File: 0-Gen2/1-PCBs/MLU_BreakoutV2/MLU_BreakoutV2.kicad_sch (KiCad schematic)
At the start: 17 parts, among them J1 SBH11-PBPC-D10-ST-BK, J2 SBH11-PBPC-D10-ST-BK, U1 Teensy4.1

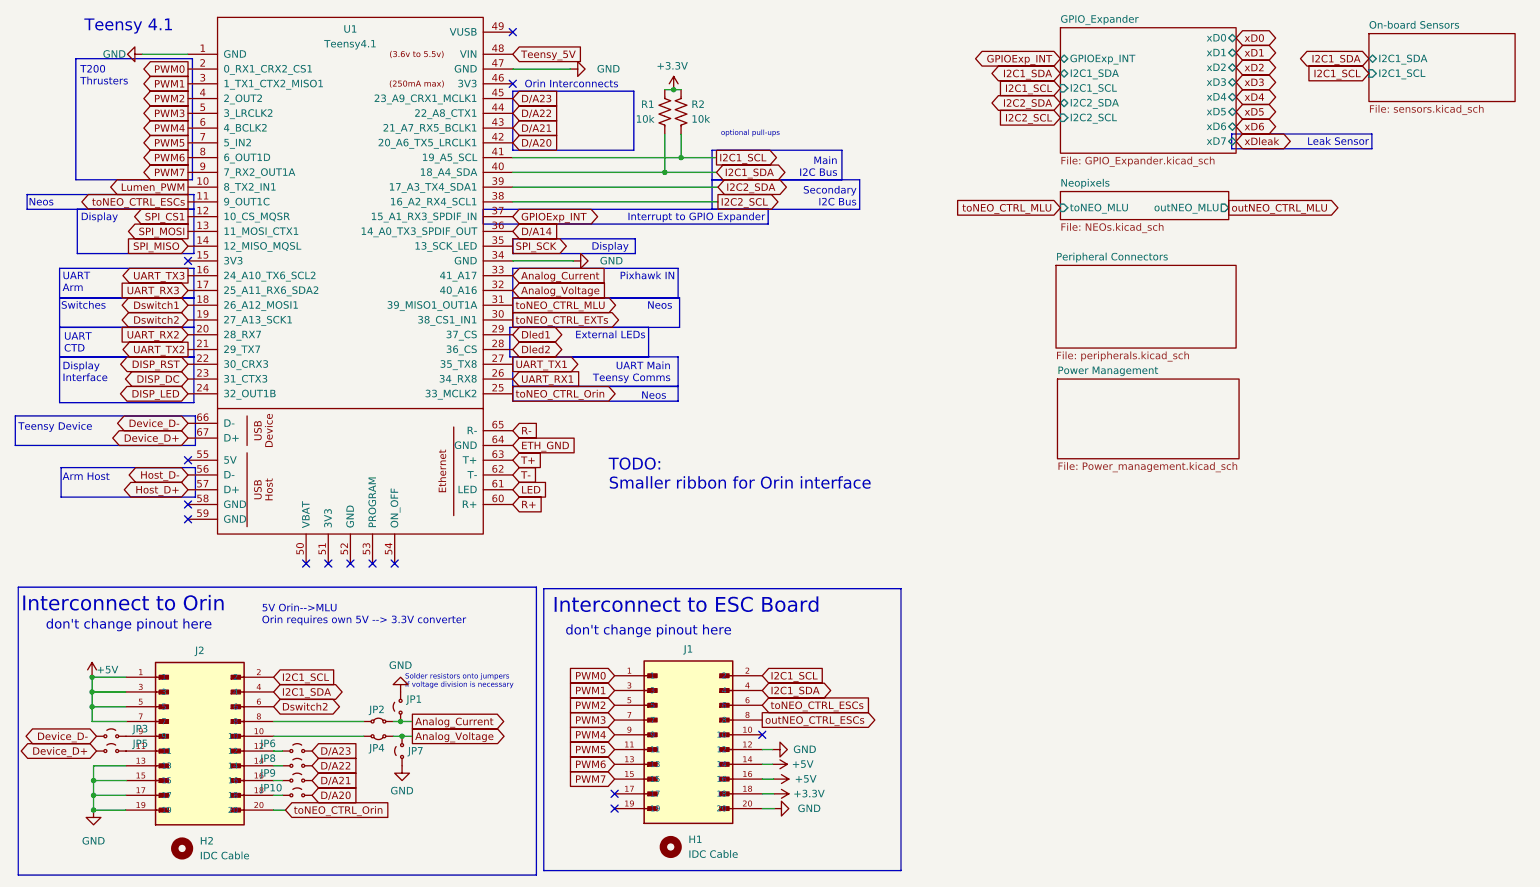
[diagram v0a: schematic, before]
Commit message: [bugfix] rescued footprints
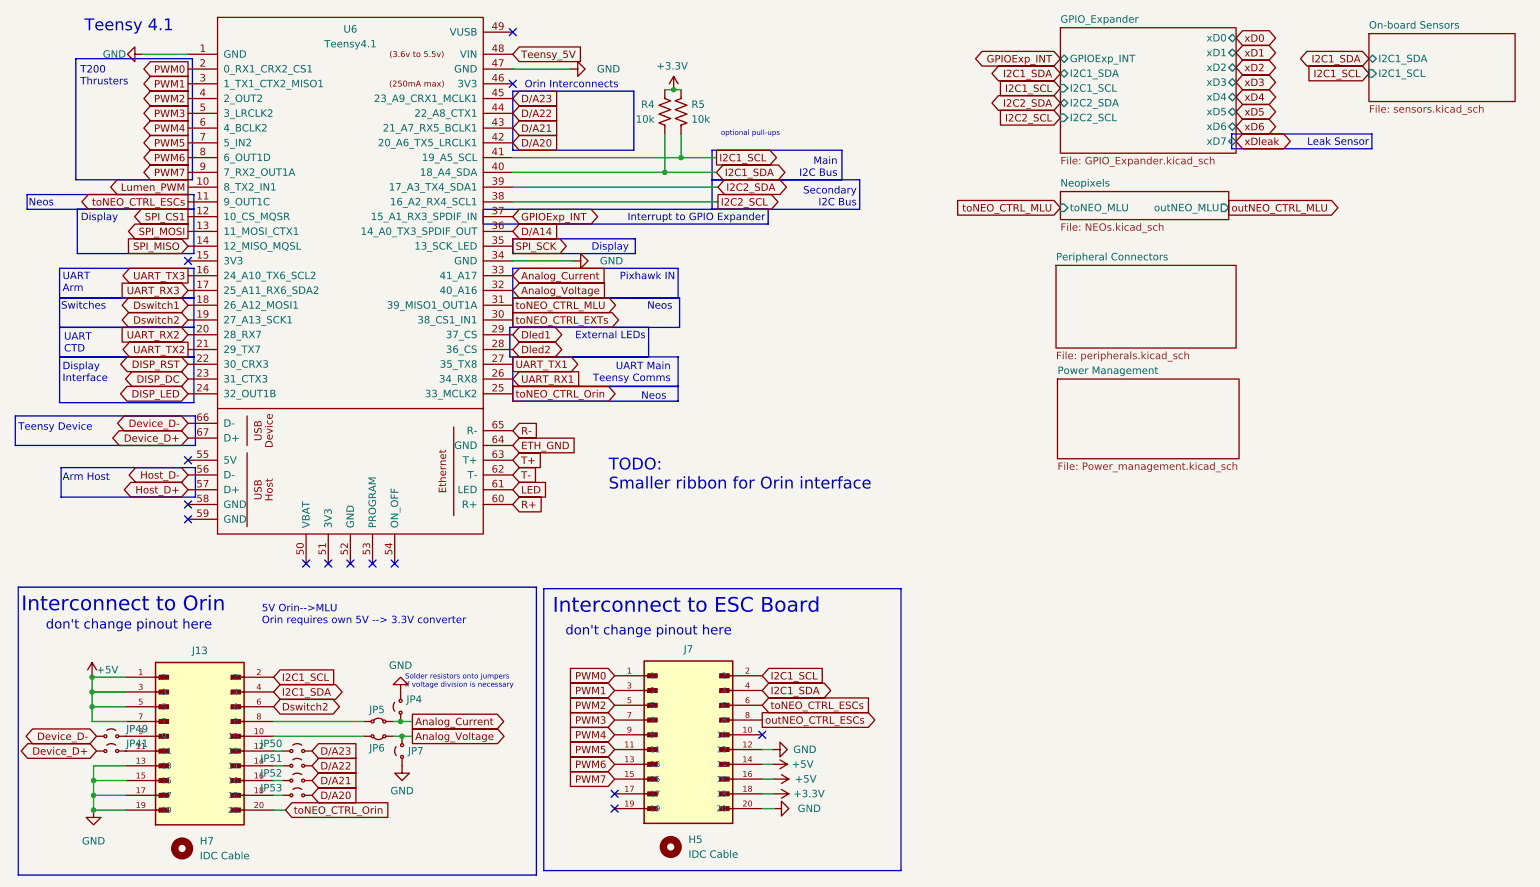
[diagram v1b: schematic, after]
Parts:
- renumbered H1 to H5, H2 to H7, J2 to J13, J1 to J7, JP1 to JP4, JP5 to JP41, JP3 to JP49, JP2 to JP5, JP6 to JP50, JP8 to JP51, JP9 to JP52, JP10 to JP53, JP4 to JP6, R1 to R4, R2 to R5, U1 to U6
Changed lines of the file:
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@@
 		(dnp no)
 		(fields_autoplaced yes)
-		(property "Reference" "#PWR04"
+		(property "Reference" "#PWR039"
 			(at 116.84 56.388 0)
 			(effects
@@
 			(project "MLU_BreakoutV2"
 				(path "/55121ba7-5d22-4fe3-93aa-7f76d75b410c"
-					(reference "#PWR04")
+					(reference "#PWR039")
 					(unit 1)
 				)
@@
 		(on_board yes)
 		(dnp no)
-		(property "Reference" "U1"
+		(property "Reference" "U6"
 			(at 72.136 16.51 0)
 			(effects
@@
 			(project "MLU_BreakoutV2"
 				(path "/55121ba7-5d22-4fe3-93aa-7f76d75b410c"
-					(reference "U1")
+					(reference "U6")
 					(unit 1)
 				)
@@
 		(on_board yes)
 		(dnp no)
-		(property "Reference" "#PWR03"
+		(property "Reference" "#PWR027"
 			(at 127.762 30.988 0)
 			(effects
@@
 			(project "MLU_BreakoutV2"
 				(path "/55121ba7-5d22-4fe3-93aa-7f76d75b410c"
-					(reference "#PWR03")
+					(reference "#PWR027")
 					(unit 1)
 				)
@@
 		(on_board yes)
 		(dnp no)
-		(property "Reference" "R1"
+		(property "Reference" "R4"
 			(at 124.46 29.4639 0)
 			(effects
@@
 			(project "MLU_BreakoutV2"
 				(path "/55121ba7-5d22-4fe3-93aa-7f76d75b410c"
-					(reference "R1")
+					(reference "R4")
 					(unit 1)
 				)
@@
 		(dnp no)
 		(fields_autoplaced yes)
-		(property "Reference" "H2"
+		(property "Reference" "H7"
 			(at 46.228 156.2099 0)
 			(effects
@@
 			(project "MLU_BreakoutV2"
 				(path "/55121ba7-5d22-4fe3-93aa-7f76d75b410c"
-					(reference "H2")
+					(reference "H7")
 					(unit 1)
 				)
@@
 		(dnp no)
 		(fields_autoplaced yes)
-		(property "Reference" "#PWR09"
+		(property "Reference" "#PWR063"
 			(at 81.026 149.606 0)
 			(effects
@@
 			(project ""
 				(path "/55121ba7-5d22-4fe3-93aa-7f76d75b410c"
-					(reference "#PWR09")
+					(reference "#PWR063")
 					(unit 1)
 				)
@@
 		(dnp no)
 		(fields_autoplaced yes)
-		(property "Reference" "#PWR06"
+		(property "Reference" "#PWR061"
 			(at 80.772 124.206 0)
 			(effects
@@
 			(project ""
 				(path "/55121ba7-5d22-4fe3-93aa-7f76d75b410c"
-					(reference "#PWR06")
+					(reference "#PWR061")
 					(unit 1)
 				)
@@
 		(dnp no)
 		(fields_autoplaced yes)
-		(property "Reference" "#PWR010"
+		(property "Reference" "#PWR030"
 			(at 141.224 145.542 0)
 			(effects
@@
 			(project "MLU_BreakoutV2"
 				(path "/55121ba7-5d22-4fe3-93aa-7f76d75b410c"
-					(reference "#PWR010")
+					(reference "#PWR030")
 					(unit 1)
 				)
@@
 		(on_board yes)
 		(dnp no)
-		(property "Reference" "JP2"
+		(property "Reference" "JP5"
 			(at 76.708 133.604 0)
 			(effects
@@
 			(project ""
 				(path "/55121ba7-5d22-4fe3-93aa-7f76d75b410c"
-					(reference "JP2")
+					(reference "JP5")
 					(unit 1)
 				)
@@
 		(on_board yes)
 		(dnp no)
-		(property "Reference" "#PWR05"
+		(property "Reference" "#PWR060"
 			(at 27.686 131.826 0)
 			(effects
@@
 			(project "MLU_BreakoutV2"
 				(path "/55121ba7-5d22-4fe3-93aa-7f76d75b410c"
-					(reference "#PWR05")
+					(reference "#PWR060")
 					(unit 1)
 				)
@@
 		(on_board yes)
 		(dnp no)
-		(property "Reference" "JP6"
+		(property "Reference" "JP50"
 			(at 56.642 139.446 0)
 			(effects
@@
 			(project "MLU_BreakoutV2"
 				(path "/55121ba7-5d22-4fe3-93aa-7f76d75b410c"
-					(reference "JP6")
+					(reference "JP50")
 					(unit 1)
 				)
@@
 		(dnp no)
 		(fields_autoplaced yes)
-		(property "Reference" "#PWR07"
+		(property "Reference" "#PWR028"
 			(at 151.13 140.462 0)
 			(effects
@@
 			(project "MLU_BreakoutV2"
 				(path "/55121ba7-5d22-4fe3-93aa-7f76d75b410c"
-					(reference "#PWR07")
+					(reference "#PWR028")
 					(unit 1)
 				)
@@
 		(on_board yes)
 		(dnp no)
-		(property "Reference" "JP1"
+		(property "Reference" "JP4"
 			(at 81.788 131.826 90)
 			(effects
@@
 			(project ""
 				(path "/55121ba7-5d22-4fe3-93aa-7f76d75b410c"
-					(reference "JP1")
+					(reference "JP4")
 					(unit 1)
 				)
@@
 		(on_board yes)
 		(dnp no)
-		(property "Reference" "R2"
+		(property "Reference" "R5"
 			(at 130.81 29.4639 0)
 			(effects
@@
 			(project "MLU_BreakoutV2"
 				(path "/55121ba7-5d22-4fe3-93aa-7f76d75b410c"
-					(reference "R2")
+					(reference "R5")
 					(unit 1)
 				)
@@
 		(on_board yes)
 		(dnp no)
-		(property "Reference" "J2"
+		(property "Reference" "J13"
 			(at 46.228 123.444 0)
 			(effects
@@
 			(project "MLU_BreakoutV2"
 				(path "/55121ba7-5d22-4fe3-93aa-7f76d75b410c"
-					(reference "J2")
+					(reference "J13")
 					(unit 1)
 				)
@@
 		(on_board yes)
 		(dnp no)
-		(property "Reference" "#PWR02"
+		(property "Reference" "#PWR026"
 			(at 116.332 23.368 0)
 			(effects
@@
 			(project "MLU_BreakoutV2"
 				(path "/55121ba7-5d22-4fe3-93aa-7f76d75b410c"
-					(reference "#PWR02")
+					(reference "#PWR026")
 					(unit 1)
 				)
@@
 		(on_board yes)
 		(dnp no)
-		(property "Reference" "JP10"
+		(property "Reference" "JP53"
 			(at 56.642 147.066 0)
 			(effects
@@
 			(project "MLU_BreakoutV2"
 				(path "/55121ba7-5d22-4fe3-93aa-7f76d75b410c"
-					(reference "JP10")
+					(reference "JP53")
 					(unit 1)
 				)
@@
 		(on_board yes)
 		(dnp no)
-		(property "Reference" "J1"
+		(property "Reference" "J7"
 			(at 130.302 123.19 0)
 			(effects
@@
 			(project "MLU_BreakoutV2"
 				(path "/55121ba7-5d22-4fe3-93aa-7f76d75b410c"
-					(reference "J1")
+					(reference "J7")
 					(unit 1)
 				)
@@
 		(on_board yes)
 		(dnp no)
-		(property "Reference" "JP4"
+		(property "Reference" "JP6"
 			(at 76.708 140.208 0)
 			(effects
@@
 			(project "MLU_BreakoutV2"
 				(path "/55121ba7-5d22-4fe3-93aa-7f76d75b410c"
-					(reference "JP4")
+					(reference "JP6")
 					(unit 1)
 				)
@@
 		(on_board yes)
 		(dnp no)
-		(property "Reference" "JP8"
+		(property "Reference" "JP51"
 			(at 56.642 141.986 0)
 			(effects
@@
 			(project "MLU_BreakoutV2"
 				(path "/55121ba7-5d22-4fe3-93aa-7f76d75b410c"
-					(reference "JP8")
+					(reference "JP51")
 					(unit 1)
 				)
@@
 		(on_board yes)
 		(dnp no)
-		(property "Reference" "JP3"
+		(property "Reference" "JP49"
 			(at 37.338 136.906 0)
 			(effects
@@
 			(project "MLU_BreakoutV2"
 				(path "/55121ba7-5d22-4fe3-93aa-7f76d75b410c"
-					(reference "JP3")
+					(reference "JP49")
 					(unit 1)
 				)
@@
 		(dnp no)
 		(fields_autoplaced yes)
-		(property "Reference" "#PWR012"
+		(property "Reference" "#PWR034"
 			(at 151.384 150.622 0)
 			(effects
@@
 			(project "MLU_BreakoutV2"
 				(path "/55121ba7-5d22-4fe3-93aa-7f76d75b410c"
-					(reference "#PWR012")
+					(reference "#PWR034")
 					(unit 1)
 				)
@@
 		(dnp no)
 		(fields_autoplaced yes)
-		(property "Reference" "#PWR01"
+		(property "Reference" "#PWR025"
 			(at 29.972 20.828 0)
 			(effects
@@
 			(project ""
 				(path "/55121ba7-5d22-4fe3-93aa-7f76d75b410c"
-					(reference "#PWR01")
+					(reference "#PWR025")
 					(unit 1)
 				)
@@
 		(on_board yes)
 		(dnp no)
-		(property "Reference" "JP5"
+		(property "Reference" "JP41"
 			(at 37.338 139.446 0)
 			(effects
@@
 			(project "MLU_BreakoutV2"
 				(path "/55121ba7-5d22-4fe3-93aa-7f76d75b410c"
-					(reference "JP5")
+					(reference "JP41")
 					(unit 1)
 				)
@@
 		(dnp no)
 		(fields_autoplaced yes)
-		(property "Reference" "#PWR013"
+		(property "Reference" "#PWR064"
 			(at 27.94 157.226 0)
 			(effects
@@
 			(project "MLU_BreakoutV2"
 				(path "/55121ba7-5d22-4fe3-93aa-7f76d75b410c"
-					(reference "#PWR013")
+					(reference "#PWR064")
 					(unit 1)
 				)
@@
 		(dnp no)
 		(fields_autoplaced yes)
-		(property "Reference" "#PWR011"
+		(property "Reference" "#PWR032"
 			(at 141.224 148.082 0)
 			(effects
@@
 			(project "MLU_BreakoutV2"
 				(path "/55121ba7-5d22-4fe3-93aa-7f76d75b410c"
-					(reference "#PWR011")
+					(reference "#PWR032")
 					(unit 1)
 				)
@@
 		(dnp no)
 		(fields_autoplaced yes)
-		(property "Reference" "H1"
+		(property "Reference" "H5"
 			(at 130.302 155.9559 0)
 			(effects
@@
 			(project "MLU_BreakoutV2"
 				(path "/55121ba7-5d22-4fe3-93aa-7f76d75b410c"
-					(reference "H1")
+					(reference "H5")
 					(unit 1)
 				)
@@
 		(dnp no)
 		(fields_autoplaced yes)
-		(property "Reference" "#PWR08"
+		(property "Reference" "#PWR029"
 			(at 140.97 143.002 0)
 			(effects
@@
 			(project "MLU_BreakoutV2"
 				(path "/55121ba7-5d22-4fe3-93aa-7f76d75b410c"
-					(reference "#PWR08")
+					(reference "#PWR029")
 					(unit 1)
 				)
@@
 		(on_board yes)
 		(dnp no)
-		(property "Reference" "JP9"
+		(property "Reference" "JP52"
 			(at 56.642 144.526 0)
 			(effects
@@
 			(project "MLU_BreakoutV2"
 				(path "/55121ba7-5d22-4fe3-93aa-7f76d75b410c"
-					(reference "JP9")
+					(reference "JP52")
 					(unit 1)
 				)

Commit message: before restructure
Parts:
- renumbered H5 to H1, H7 to H2, J7 to J1, J13 to J2, JP4 to JP1, JP53 to JP10, JP5 to JP2, JP49 to JP3, JP6 to JP4, JP41 to JP5, JP50 to JP6, JP51 to JP8, JP52 to JP9, R4 to R1, R5 to R2, U6 to U1
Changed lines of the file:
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@@
 		(dnp no)
 		(fields_autoplaced yes)
-		(property "Reference" "#PWR039"
+		(property "Reference" "#PWR04"
 			(at 116.84 56.388 0)
 			(effects
@@
 			(project "MLU_BreakoutV2"
 				(path "/55121ba7-5d22-4fe3-93aa-7f76d75b410c"
-					(reference "#PWR039")
+					(reference "#PWR04")
 					(unit 1)
 				)
@@
 		(on_board yes)
 		(dnp no)
-		(property "Reference" "U6"
+		(property "Reference" "U1"
 			(at 72.136 16.51 0)
 			(effects
@@
 			(project "MLU_BreakoutV2"
 				(path "/55121ba7-5d22-4fe3-93aa-7f76d75b410c"
-					(reference "U6")
+					(reference "U1")
 					(unit 1)
 				)
@@
 		(on_board yes)
 		(dnp no)
-		(property "Reference" "#PWR027"
+		(property "Reference" "#PWR03"
 			(at 127.762 30.988 0)
 			(effects
@@
 			(project "MLU_BreakoutV2"
 				(path "/55121ba7-5d22-4fe3-93aa-7f76d75b410c"
-					(reference "#PWR027")
+					(reference "#PWR03")
 					(unit 1)
 				)
@@
 		(on_board yes)
 		(dnp no)
-		(property "Reference" "R4"
+		(property "Reference" "R1"
 			(at 124.46 29.4639 0)
 			(effects
@@
 			(project "MLU_BreakoutV2"
 				(path "/55121ba7-5d22-4fe3-93aa-7f76d75b410c"
-					(reference "R4")
+					(reference "R1")
 					(unit 1)
 				)
@@
 		(dnp no)
 		(fields_autoplaced yes)
-		(property "Reference" "H7"
+		(property "Reference" "H2"
 			(at 46.228 156.2099 0)
 			(effects
@@
 			(project "MLU_BreakoutV2"
 				(path "/55121ba7-5d22-4fe3-93aa-7f76d75b410c"
-					(reference "H7")
+					(reference "H2")
 					(unit 1)
 				)
@@
 		(dnp no)
 		(fields_autoplaced yes)
-		(property "Reference" "#PWR063"
+		(property "Reference" "#PWR09"
 			(at 81.026 149.606 0)
 			(effects
@@
 			(project ""
 				(path "/55121ba7-5d22-4fe3-93aa-7f76d75b410c"
-					(reference "#PWR063")
+					(reference "#PWR09")
 					(unit 1)
 				)
@@
 		(dnp no)
 		(fields_autoplaced yes)
-		(property "Reference" "#PWR061"
+		(property "Reference" "#PWR06"
 			(at 80.772 124.206 0)
 			(effects
@@
 			(project ""
 				(path "/55121ba7-5d22-4fe3-93aa-7f76d75b410c"
-					(reference "#PWR061")
+					(reference "#PWR06")
 					(unit 1)
 				)
@@
 		(dnp no)
 		(fields_autoplaced yes)
-		(property "Reference" "#PWR030"
+		(property "Reference" "#PWR010"
 			(at 141.224 145.542 0)
 			(effects
@@
 			(project "MLU_BreakoutV2"
 				(path "/55121ba7-5d22-4fe3-93aa-7f76d75b410c"
-					(reference "#PWR030")
+					(reference "#PWR010")
 					(unit 1)
 				)
@@
 		(on_board yes)
 		(dnp no)
-		(property "Reference" "JP5"
+		(property "Reference" "JP2"
 			(at 76.708 133.604 0)
 			(effects
@@
 			(project ""
 				(path "/55121ba7-5d22-4fe3-93aa-7f76d75b410c"
-					(reference "JP5")
+					(reference "JP2")
 					(unit 1)
 				)
@@
 		(on_board yes)
 		(dnp no)
-		(property "Reference" "#PWR060"
+		(property "Reference" "#PWR05"
 			(at 27.686 131.826 0)
 			(effects
@@
 			(project "MLU_BreakoutV2"
 				(path "/55121ba7-5d22-4fe3-93aa-7f76d75b410c"
-					(reference "#PWR060")
+					(reference "#PWR05")
 					(unit 1)
 				)
@@
 		(on_board yes)
 		(dnp no)
-		(property "Reference" "JP50"
+		(property "Reference" "JP6"
 			(at 56.642 139.446 0)
 			(effects
@@
 			(project "MLU_BreakoutV2"
 				(path "/55121ba7-5d22-4fe3-93aa-7f76d75b410c"
-					(reference "JP50")
+					(reference "JP6")
 					(unit 1)
 				)
@@
 		(dnp no)
 		(fields_autoplaced yes)
-		(property "Reference" "#PWR028"
+		(property "Reference" "#PWR07"
 			(at 151.13 140.462 0)
 			(effects
@@
 			(project "MLU_BreakoutV2"
 				(path "/55121ba7-5d22-4fe3-93aa-7f76d75b410c"
-					(reference "#PWR028")
+					(reference "#PWR07")
 					(unit 1)
 				)
@@
 		(on_board yes)
 		(dnp no)
-		(property "Reference" "JP4"
+		(property "Reference" "JP1"
 			(at 81.788 131.826 90)
 			(effects
@@
 			(project ""
 				(path "/55121ba7-5d22-4fe3-93aa-7f76d75b410c"
-					(reference "JP4")
+					(reference "JP1")
 					(unit 1)
 				)
@@
 		(on_board yes)
 		(dnp no)
-		(property "Reference" "R5"
+		(property "Reference" "R2"
 			(at 130.81 29.4639 0)
 			(effects
@@
 			(project "MLU_BreakoutV2"
 				(path "/55121ba7-5d22-4fe3-93aa-7f76d75b410c"
-					(reference "R5")
+					(reference "R2")
 					(unit 1)
 				)
@@
 		(on_board yes)
 		(dnp no)
-		(property "Reference" "J13"
+		(property "Reference" "J2"
 			(at 46.228 123.444 0)
 			(effects
@@
 			(project "MLU_BreakoutV2"
 				(path "/55121ba7-5d22-4fe3-93aa-7f76d75b410c"
-					(reference "J13")
+					(reference "J2")
 					(unit 1)
 				)
@@
 		(on_board yes)
 		(dnp no)
-		(property "Reference" "#PWR026"
+		(property "Reference" "#PWR02"
 			(at 116.332 23.368 0)
 			(effects
@@
 			(project "MLU_BreakoutV2"
 				(path "/55121ba7-5d22-4fe3-93aa-7f76d75b410c"
-					(reference "#PWR026")
+					(reference "#PWR02")
 					(unit 1)
 				)
@@
 		(on_board yes)
 		(dnp no)
-		(property "Reference" "JP53"
+		(property "Reference" "JP10"
 			(at 56.642 147.066 0)
 			(effects
@@
 			(project "MLU_BreakoutV2"
 				(path "/55121ba7-5d22-4fe3-93aa-7f76d75b410c"
-					(reference "JP53")
+					(reference "JP10")
 					(unit 1)
 				)
@@
 		(on_board yes)
 		(dnp no)
-		(property "Reference" "J7"
+		(property "Reference" "J1"
 			(at 130.302 123.19 0)
 			(effects
@@
 			(project "MLU_BreakoutV2"
 				(path "/55121ba7-5d22-4fe3-93aa-7f76d75b410c"
-					(reference "J7")
+					(reference "J1")
 					(unit 1)
 				)
@@
 		(on_board yes)
 		(dnp no)
-		(property "Reference" "JP6"
+		(property "Reference" "JP4"
 			(at 76.708 140.208 0)
 			(effects
@@
 			(project "MLU_BreakoutV2"
 				(path "/55121ba7-5d22-4fe3-93aa-7f76d75b410c"
-					(reference "JP6")
+					(reference "JP4")
 					(unit 1)
 				)
@@
 		(on_board yes)
 		(dnp no)
-		(property "Reference" "JP51"
+		(property "Reference" "JP8"
 			(at 56.642 141.986 0)
 			(effects
@@
 			(project "MLU_BreakoutV2"
 				(path "/55121ba7-5d22-4fe3-93aa-7f76d75b410c"
-					(reference "JP51")
+					(reference "JP8")
 					(unit 1)
 				)
@@
 		(on_board yes)
 		(dnp no)
-		(property "Reference" "JP49"
+		(property "Reference" "JP3"
 			(at 37.338 136.906 0)
 			(effects
@@
 			(project "MLU_BreakoutV2"
 				(path "/55121ba7-5d22-4fe3-93aa-7f76d75b410c"
-					(reference "JP49")
+					(reference "JP3")
 					(unit 1)
 				)
@@
 		(dnp no)
 		(fields_autoplaced yes)
-		(property "Reference" "#PWR034"
+		(property "Reference" "#PWR012"
 			(at 151.384 150.622 0)
 			(effects
@@
 			(project "MLU_BreakoutV2"
 				(path "/55121ba7-5d22-4fe3-93aa-7f76d75b410c"
-					(reference "#PWR034")
+					(reference "#PWR012")
 					(unit 1)
 				)
@@
 		(dnp no)
 		(fields_autoplaced yes)
-		(property "Reference" "#PWR025"
+		(property "Reference" "#PWR01"
 			(at 29.972 20.828 0)
 			(effects
@@
 			(project ""
 				(path "/55121ba7-5d22-4fe3-93aa-7f76d75b410c"
-					(reference "#PWR025")
+					(reference "#PWR01")
 					(unit 1)
 				)
@@
 		(on_board yes)
 		(dnp no)
-		(property "Reference" "JP41"
+		(property "Reference" "JP5"
 			(at 37.338 139.446 0)
 			(effects
@@
 			(project "MLU_BreakoutV2"
 				(path "/55121ba7-5d22-4fe3-93aa-7f76d75b410c"
-					(reference "JP41")
+					(reference "JP5")
 					(unit 1)
 				)
@@
 		(dnp no)
 		(fields_autoplaced yes)
-		(property "Reference" "#PWR064"
+		(property "Reference" "#PWR013"
 			(at 27.94 157.226 0)
 			(effects
@@
 			(project "MLU_BreakoutV2"
 				(path "/55121ba7-5d22-4fe3-93aa-7f76d75b410c"
-					(reference "#PWR064")
+					(reference "#PWR013")
 					(unit 1)
 				)
@@
 		(dnp no)
 		(fields_autoplaced yes)
-		(property "Reference" "#PWR032"
+		(property "Reference" "#PWR011"
 			(at 141.224 148.082 0)
 			(effects
@@
 			(project "MLU_BreakoutV2"
 				(path "/55121ba7-5d22-4fe3-93aa-7f76d75b410c"
-					(reference "#PWR032")
+					(reference "#PWR011")
 					(unit 1)
 				)
@@
 		(dnp no)
 		(fields_autoplaced yes)
-		(property "Reference" "H5"
+		(property "Reference" "H1"
 			(at 130.302 155.9559 0)
 			(effects
@@
 			(project "MLU_BreakoutV2"
 				(path "/55121ba7-5d22-4fe3-93aa-7f76d75b410c"
-					(reference "H5")
+					(reference "H1")
 					(unit 1)
 				)
@@
 		(dnp no)
 		(fields_autoplaced yes)
-		(property "Reference" "#PWR029"
+		(property "Reference" "#PWR08"
 			(at 140.97 143.002 0)
 			(effects
@@
 			(project "MLU_BreakoutV2"
 				(path "/55121ba7-5d22-4fe3-93aa-7f76d75b410c"
-					(reference "#PWR029")
+					(reference "#PWR08")
 					(unit 1)
 				)
@@
 		(on_board yes)
 		(dnp no)
-		(property "Reference" "JP52"
+		(property "Reference" "JP9"
 			(at 56.642 144.526 0)
 			(effects
@@
 			(project "MLU_BreakoutV2"
 				(path "/55121ba7-5d22-4fe3-93aa-7f76d75b410c"
-					(reference "JP52")
+					(reference "JP9")
 					(unit 1)
 				)
